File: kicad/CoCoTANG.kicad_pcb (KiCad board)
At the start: 2 copper layers, 187.5 x 58.4 mm, 84 parts, among them J1 CPU, J13 CoCo_Cart, J14 PIA0_IN, J15 PIA1_IN, J18 CMP_IN, J2 ADDRMUX_OUT, J21 CMP_OUT, J23 TRG, J28 ADDRMUX, J3 ADDRMUX_IN, J4 PIA0, J6 CLK, J7 AV_HEADER, J8 PIA0_OUT, Q2 MMBT3904-TP, Q4 MMBT3904-TP, Q5 MMBT3904-TP, Q7 MMBT3904-TP, Q8 MMBT3904-TP, Q9 MMBT3904-TP, U1 74HC138, U10 74LVC245, U11 74LVC245, U12 74LVC245, U2 AT28C64B-15PU, U22 74HC11, U3 74HC139, U5 Tang_Nano_20k, U7 74HC30, U8 74LVC245, U9 74HC245

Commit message: kicad changes
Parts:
- added C13, C14, C15, C16, C18, C19: 104, Capacitor_SMD:C_0805_2012Metric_Pad1.18x1.45mm_HandSolder, B.Cu at (0.00, 0.00)
- added D4: SS14, Diode_SMD:D_SMA, F.Cu at (0.00, 0.00)
- added H1: MountingHole, MountingHole:MountingHole_4.3mm_M4, F.Cu at (0.00, 0.00)
- added J10: AV_HEADER, Connector_PinSocket_2.54mm:PinSocket_1x06_P2.54mm_Vertical, F.Cu at (0.00, 0.00)
- added J11: CLK, Connector_PinSocket_2.54mm:PinSocket_1x01_P2.54mm_Vertical, F.Cu at (0.00, 0.00)
- added J12: PIA1_IN, Connector_PinHeader_2.54mm:PinHeader_1x02_P2.54mm_Vertical, F.Cu at (0.00, 0.00)
- added J16: PIA0_IN, Connector_PinHeader_2.54mm:PinHeader_1x03_P2.54mm_Vertical, F.Cu at (0.00, 0.00)
- added J17: ADDRMUX_IN, Connector_PinHeader_2.54mm:PinHeader_1x07_P2.54mm_Vertical, F.Cu at (0.00, 0.00)
- added J19: CPU, FPGA_Common:DIP-40_W15.24mm-OVERSIZED, F.Cu at (0.00, 0.00)
- added J5: EXTKEY, Connector_PinSocket_2.54mm:PinSocket_1x05_P2.54mm_Vertical, F.Cu at (0.00, 0.00)
- added J9: EXTKEY_IN, Connector_PinSocket_2.54mm:PinSocket_1x05_P2.54mm_Vertical, F.Cu at (0.00, 0.00)
- added Q1, Q3, Q6: MMBT3904-TP, FPGA_Common:SOT-23_MCC, F.Cu at (0.00, 0.00)
- added R13, R20, R21, R22: 4.7K, Resistor_SMD:R_0805_2012Metric_Pad1.20x1.40mm_HandSolder, F.Cu at (0.00, 0.00)
- added R14, R15, R18: 10K, Resistor_SMD:R_0805_2012Metric_Pad1.20x1.40mm_HandSolder, F.Cu at (0.00, 0.00)
- added R25, R26: 47K, Resistor_SMD:R_0805_2012Metric_Pad1.20x1.40mm_HandSolder, F.Cu at (0.00, 0.00)
- added RN3, RN4: 4.7K, Resistor_THT:R_Array_SIP9, F.Cu at (0.00, 0.00)
- added SW1: ALT, Button_Switch_Keyboard:SW_Cherry_MX_1.00u_PCB, F.Cu at (0.00, 0.00)
- added SW2: CTRL, Button_Switch_Keyboard:SW_Cherry_MX_1.00u_PCB, F.Cu at (0.00, 0.00)
- added SW3: F1, Button_Switch_Keyboard:SW_Cherry_MX_1.00u_PCB, F.Cu at (0.00, 0.00)
- added SW4: F2, Button_Switch_Keyboard:SW_Cherry_MX_1.00u_PCB, F.Cu at (0.00, 0.00)
- added U13, U14, U15, U4: 74LVC245, Package_SO:TSSOP-20_4.4x6.5mm_P0.65mm, F.Cu at (0.00, 0.00)
- added U16: 74HCT245, Package_SO:TSSOP-20_4.4x6.5mm_P0.65mm, F.Cu at (0.00, 0.00)
- added U17: Tang_Nano_20k, FPGA_Common:Tang_Nano_20k, F.Cu at (0.00, 0.00)
- added U6: 74HCT139, Package_SO:TSSOP-16_4.4x5mm_P0.65mm, F.Cu at (0.00, 0.00)
- R19: value 47K -> 4.7K
- RN1, RN2: value R_Network08 -> 4.7K
- U1: value 74HC138 -> 74HCT138
- U22: value 74HC11 -> 74HCT11
- U3: value 74HC139 -> 74HCT139
- U7: value 74HC30 -> 74HCT30
- U9: value 74HC245 -> 74HCT245
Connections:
- net AP11 renamed PB1
- net AP12 renamed PB2
- net AP17 renamed PB7
- net AP9 renamed PA7
- net PB10/SERNT renamed PB0
- net ROW0 renamed PA0
- net ROW1 renamed PA1
- net ROW2 renamed PA2
- net ROW3 renamed PA3
- net ROW4 renamed PA4
- net ROW5 renamed PA5
- net ROW6 renamed PA6
- J4 pad 13: AP13 -> PB3
- J4 pad 14: AP14 -> PB4
- J4 pad 15: AP15 -> PB5
- J4 pad 16: AP16 -> PB6
- U22 pad 4: PIA0 -> DATADIR
- U22 pad 5: PIA1 -> +5V
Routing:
- net PA6: track 15.0 -> 94.1 mm
- net PB6: track 0.00 -> 60.6 mm
- net PB5: track 0.00 -> 44.3 mm
- net IRQ_33: track 84.2 -> 125.5 mm, vias 1 -> 0
- net S2: track 134.4 -> 93.5 mm
- net MP4_33: track 74.6 -> 115.0 mm, vias 4 -> 3
- net GND: track 620.4 -> 653.2 mm, vias 14 -> 20
- net RESET_33: track 46.1 -> 78.2 mm, vias 1 -> 0
- net PB3: track 0.00 -> 28.1 mm
- net AUDIO_33: track 93.2 -> 116.9 mm, vias 3 -> 2
- net S1: track 112.6 -> 92.7 mm
- net FIRQ_33: track 105.1 -> 86.1 mm
- net MP3_33: track 84.5 -> 69.0 mm, vias 3 -> 2
- net R/~{W}: track 143.9 -> 128.6 mm
- net ~{SLENB}: track 61.9 -> 76.1 mm, vias 2 -> 1
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- added copper zone on B.Cu, net GND
- added copper zone on F.Cu, net GND
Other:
- board size 187.5 x 58.4 mm -> 242.8 x 117.2 mm
- board text added: "COCOTANG V1.01a 2026 LUIS ANTONIOSI"
- board text added: "COCOTANG V1.01b 2026 LUIS ANTONIOSI"

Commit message: Go Live
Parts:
- removed J21: CMP_OUT, Connector_PinHeader_2.54mm:PinHeader_1x05_P2.54mm_Vertical
- added J20, J22: SUPPORT, Connector_PinSocket_2.54mm:PinSocket_1x02_P2.54mm_Vertical, F.Cu at (0.00, 0.00)
- added J24: AV, FPGA_Common:SWITCHCRAFT_57PC5F, F.Cu at (0.00, 0.00)
- J11: value CLK -> SUPPORT; footprint Connector_PinSocket_2.54mm:PinSocket_1x01_P2.54mm_Vertical -> Connector_PinSocket_2.54mm:PinSocket_1x02_P2.54mm_Vertical
- J6: value CLK -> SUPPORT; footprint Connector_PinSocket_2.54mm:PinSocket_1x01_P2.54mm_Vertical -> Connector_PinHeader_2.54mm:PinHeader_1x10_P2.54mm_Vertical
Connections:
- J11 pad 1: CLK -> unconnected-(J11-Pin_1-Pad1)
- J6 pad 1: CLK -> unconnected-(J6-Pin_1-Pad1)
- U16 pad 11: CLK -> unconnected-(U16-B7-Pad11)
- U16 pad 9: AUDIO_33 -> unconnected-(U16-A7-Pad9)
- U9 pad 11: CLK -> unconnected-(U9-B7-Pad11)
- U9 pad 9: AUDIO_33 -> unconnected-(U9-A7-Pad9)
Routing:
- net GND: track 653.2 -> 905.5 mm, vias 20 -> 27
- net +5V: track 300.5 -> 477.6 mm, vias 9 -> 8
- net +3.3V: track 286.7 -> 463.5 mm, vias 14 -> 21
- net A14: track 52.9 -> 222.6 mm, vias 1 -> 2
- net R/~{W}: track 128.6 -> 271.5 mm, vias 1 -> 6
- net MP6_33: track 73.4 -> 214.1 mm
- net FIRQ_33: track 86.1 -> 222.7 mm, vias 2 -> 3
- net A12: track 78.6 -> 208.3 mm
- net KEYINT: track 105.1 -> 231.1 mm, vias 1 -> 3
- net A11: track 66.7 -> 181.2 mm
- net A6: track 86.4 -> 198.8 mm, vias 1 -> 5
- net ~{RESET}: track 35.9 -> 144.0 mm
- net MP0_33: track 68.4 -> 174.3 mm, vias 3 -> 8
- net ~{FS_33}: track 50.6 -> 154.8 mm
- net D4_33: track 24.7 -> 125.8 mm, vias 1 -> 2
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- removed copper zone on B.Cu, net A11
- removed copper zone on F.Cu, net A11
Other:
- board size 242.8 x 117.2 mm -> 236.8 x 129.1 mm
- board text added: "COCOTANG V1.02 2026 LUIS ANTONIOSI"
- board text added: "COCOTANG V1.02a 2026 LUIS ANTONIOSI"
- board text added: "COCOTANG V1.02b 2026 LUIS ANTONIOSI"
- board text added: "G/Y B/CHR R/CVBS AUDIO 3.3V GND"
- board text removed: "AUDIO"
- board text removed: "B/CHR"
- board text removed: "COCOTANG V1.00 2026 LUIS ANTONIOSI"
- board text removed: "COCOTANG V1.01a 2026 LUIS ANTONIOSI"
- board text removed: "COCOTANG V1.01b 2026 LUIS ANTONIOSI"
- board text removed: "COMPONENT / RGB 1.1"
- board text removed: "G/Y"
- board text removed: "GND"
- board text removed: "R/CVBS"

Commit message: final boards
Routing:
- net B_CHR: track 41.0 -> 20.4 mm
- net R_CVBS: track 39.0 -> 21.4 mm, vias 1 -> 0
- net GND: track 905.5 -> 891.7 mm
- net AUDIO_RCA: track 22.9 -> 19.3 mm
- net G_Y: track 32.3 -> 28.9 mm, vias 0 -> 1
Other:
- board text added: "COCOTANG V1.02 20261043 2026 LUIS ANTONIOSI"
- board text added: "COCOTANG V1.02 20261058 2026 LUIS ANTONIOSI"
- board text removed: "COCOTANG V1.02a 2026 LUIS ANTONIOSI"
- board text removed: "COCOTANG V1.02b 2026 LUIS ANTONIOSI"

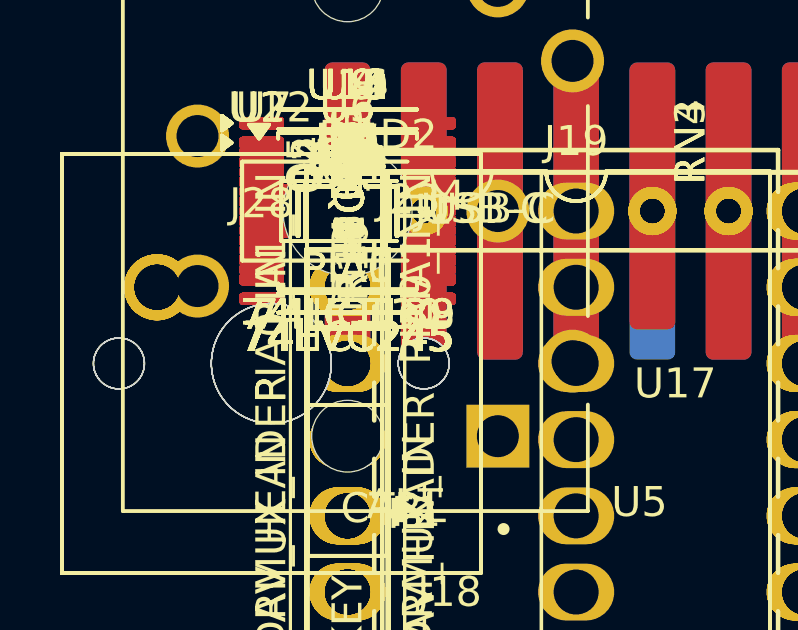
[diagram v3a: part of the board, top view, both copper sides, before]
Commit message: fix some labels
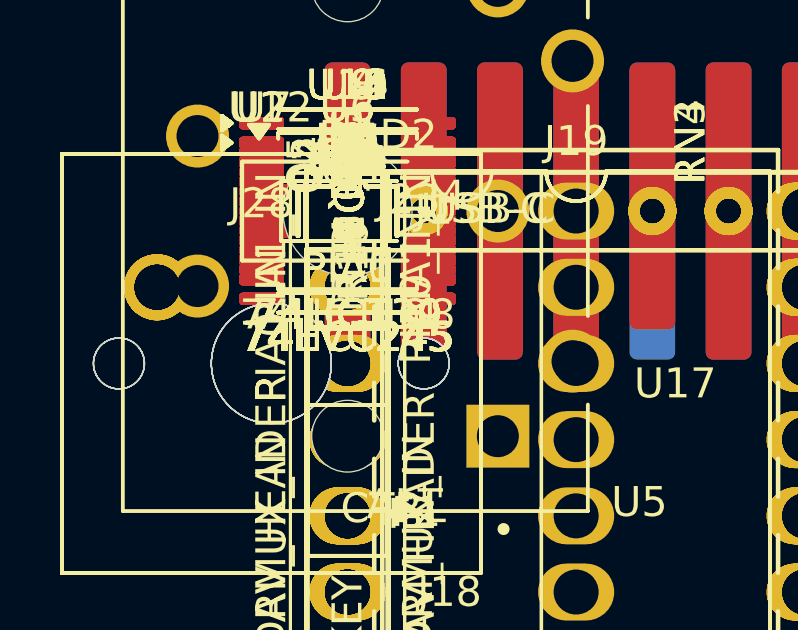
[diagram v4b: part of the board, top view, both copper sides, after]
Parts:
- U3, U6: value 74HCT139 -> 74HC139
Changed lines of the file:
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@@
 			(drillshape 0)
 			(scaleselection 1)
-			(outputdirectory "gerber_extkey")
+			(outputdirectory "gerber_main_20261058/")
 		)
 	)
@@
 			)
 		)
-		(property "Value" "74HCT139"
+		(property "Value" "74HC139"
 			(at 0 3.45 0)
 			(layer "F.SilkS")
@@
 			)
 		)
-		(property "Value" "74HCT139"
+		(property "Value" "74HC139"
 			(at 0 3.45 0)
 			(layer "F.SilkS")
@@
 		(sheetname "/")
 		(sheetfile "CoCoTANG.kicad_sch")
+		(units
+			(unit
+				(name "A")
+				(pins "1" "2" "3" "4" "5" "6" "7" "8" "16" "15" "14" "13" "12" "11" "10"
+					"9"
+				)
+			)
+		)
 		(attr through_hole)
 		(duplicate_pad_numbers_are_jumpers no)
@@
 		(sheetname "/")
 		(sheetfile "CoCoTANG.kicad_sch")
+		(units
+			(unit
+				(name "A")
+				(pins "1" "2" "3" "4" "5" "6" "7" "8" "9" "10" "11" "12" "13" "14" "15"
+					"16" "17" "18" "19" "20" "40" "39" "38" "37" "36" "35" "34" "33" "32"
+					"31" "30" "29" "28" "27" "26" "25" "24" "23" "22" "21"
+				)
+			)
+		)
 		(attr through_hole)
 		(duplicate_pad_numbers_are_jumpers no)
@@
 		(sheetname "/")
 		(sheetfile "CoCoTANG.kicad_sch")
+		(units
+			(unit
+				(name "A")
+				(pins "1" "2" "3" "4" "5" "6" "7" "8" "9" "10" "11" "12" "13" "14" "15"
+					"16" "17" "18" "19" "20" "40" "39" "38" "37" "36" "35" "34" "33" "32"
+					"31" "30" "29" "28" "27" "26" "25" "24" "23" "22" "21"
+				)
+			)
+		)
 		(attr through_hole)
 		(duplicate_pad_numbers_are_jumpers no)
@@
 		(sheetname "/")
 		(sheetfile "CoCoTANG.kicad_sch")
+		(units
+			(unit
+				(name "A")
+				(pins "1" "2" "3" "4" "5" "6" "7" "8" "9" "10" "11" "12" "13" "14" "15"
+					"16" "17" "18" "19" "20" "40" "39" "38" "37" "36" "35" "34" "33" "32"
+					"31" "30" "29" "28" "27" "26" "25" "24" "23" "22" "21"
+				)
+			)
+		)
 		(attr through_hole)
 		(duplicate_pad_numbers_are_jumpers no)

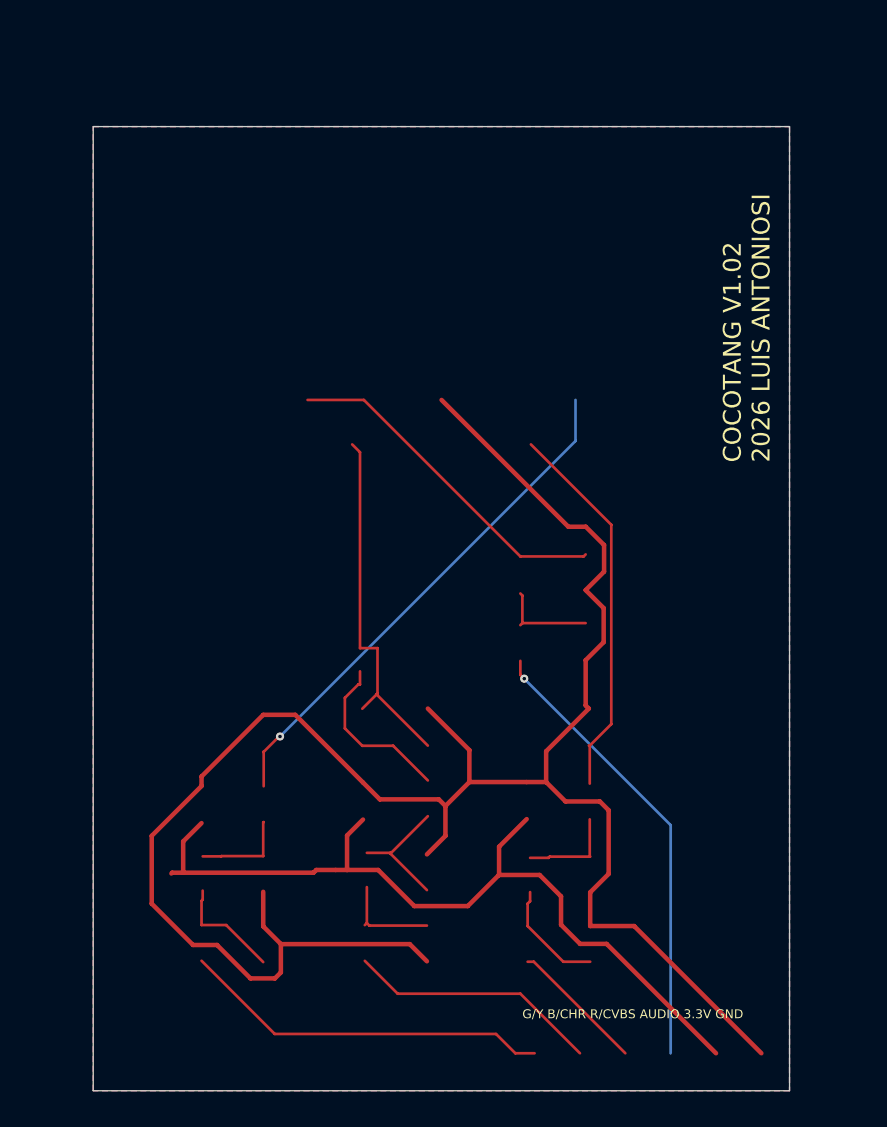
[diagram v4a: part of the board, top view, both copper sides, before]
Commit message: change video board DIN position
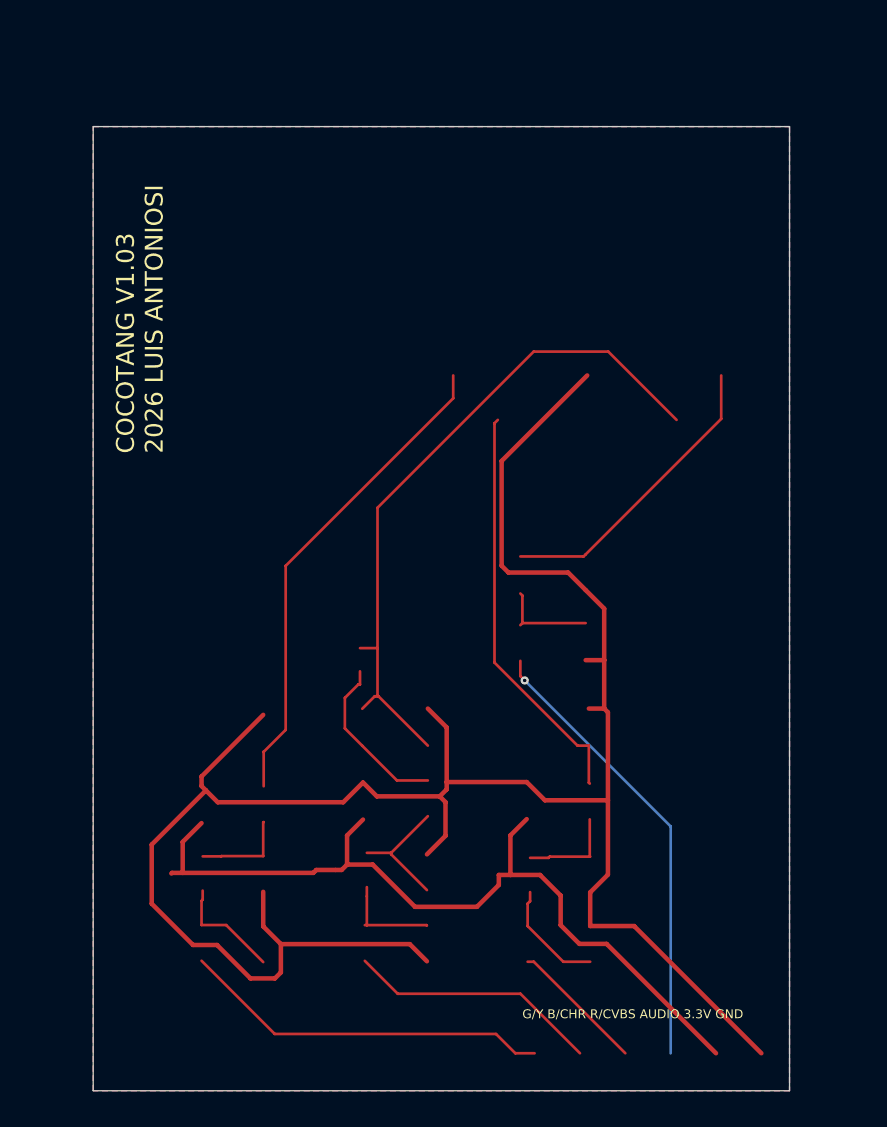
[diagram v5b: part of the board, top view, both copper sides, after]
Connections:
- J24 pad 1: AUDIO_RCA -> G_Y
- J24 pad 3: G_Y -> AUDIO_RCA
- J24 pad 4: B_CHR -> R_CVBS
- J24 pad 5: R_CVBS -> B_CHR
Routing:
- net B_CHR: track 20.4 -> 38.6 mm
- net GND: track 891.7 -> 898.5 mm
- net AUDIO_RCA: track 19.3 -> 16.9 mm
- net R_CVBS: track 21.4 -> 23.0 mm
- net G_Y: track 28.9 -> 27.4 mm, vias 1 -> 0
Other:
- board text added: "COCOTANG V1.03 2026 LUIS ANTONIOSI"
